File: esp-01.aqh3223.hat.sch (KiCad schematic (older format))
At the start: 17 parts, among them J1 AC Terminal, J2 GPIO/I2C, Q1 BC547, Q2 BC547, SW1 VCC_Switch, U1 ESP-01v090, U2 AMS1117-3.3, U3 AQH3223, U4 AQH3223

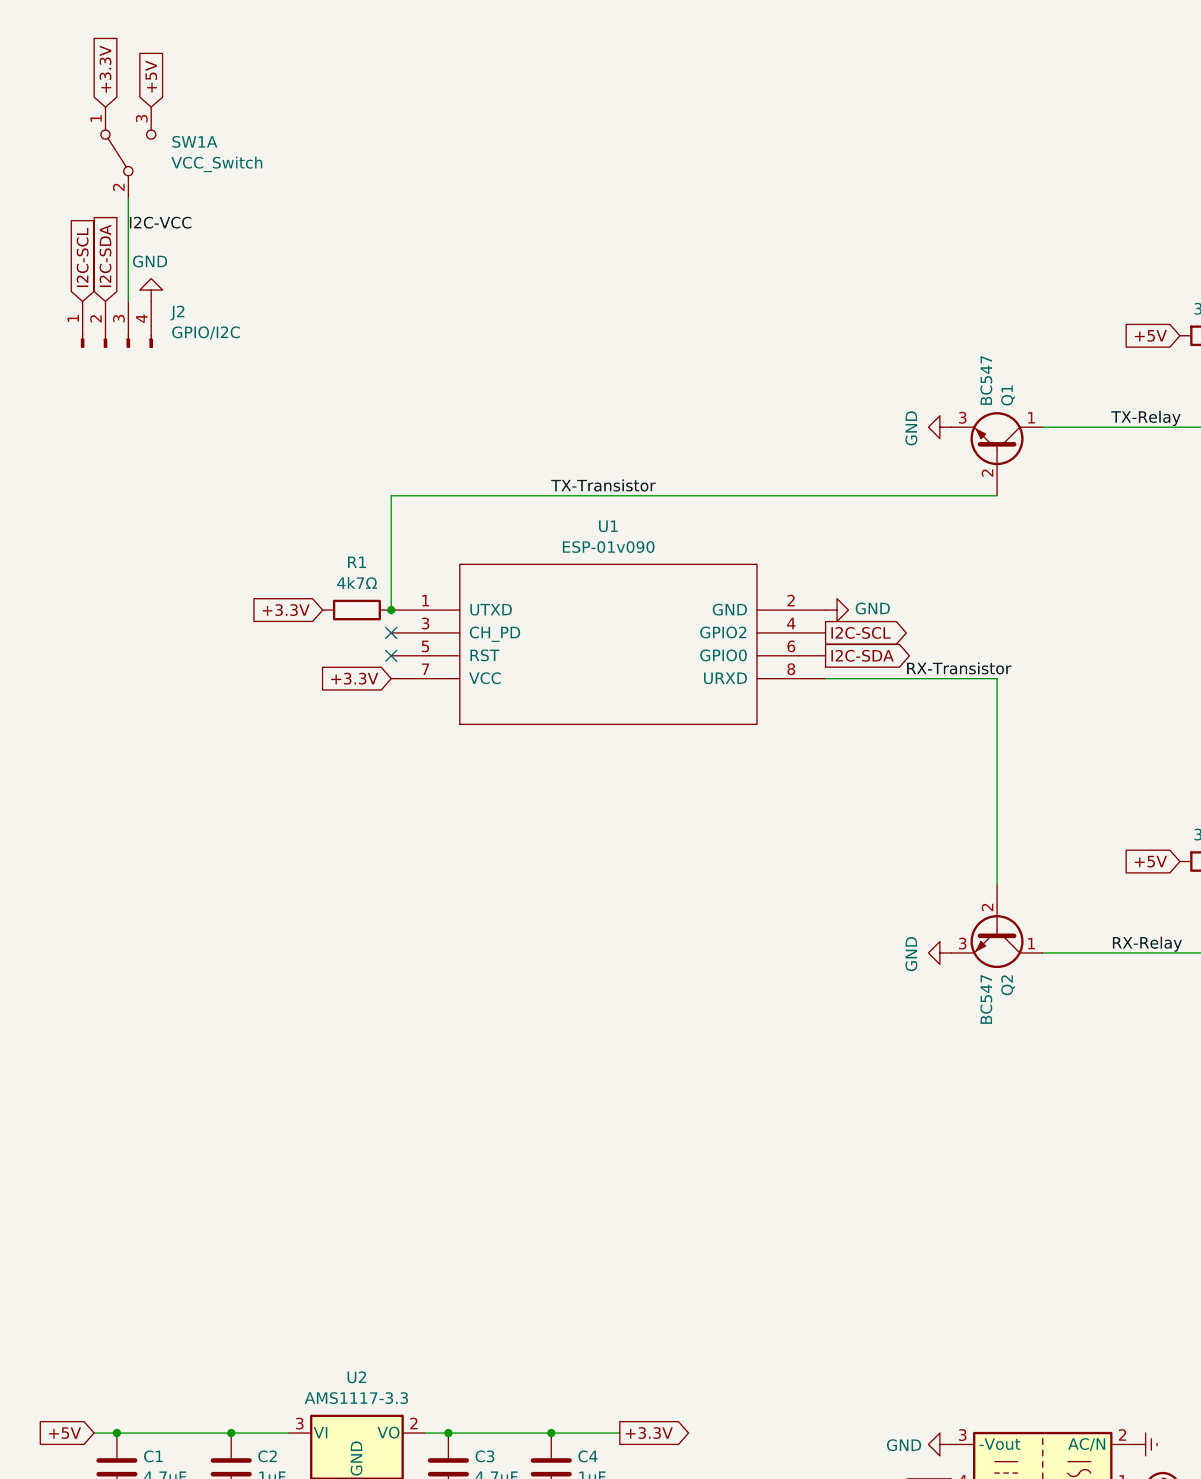
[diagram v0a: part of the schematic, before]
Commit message: fixed booting of esp-01
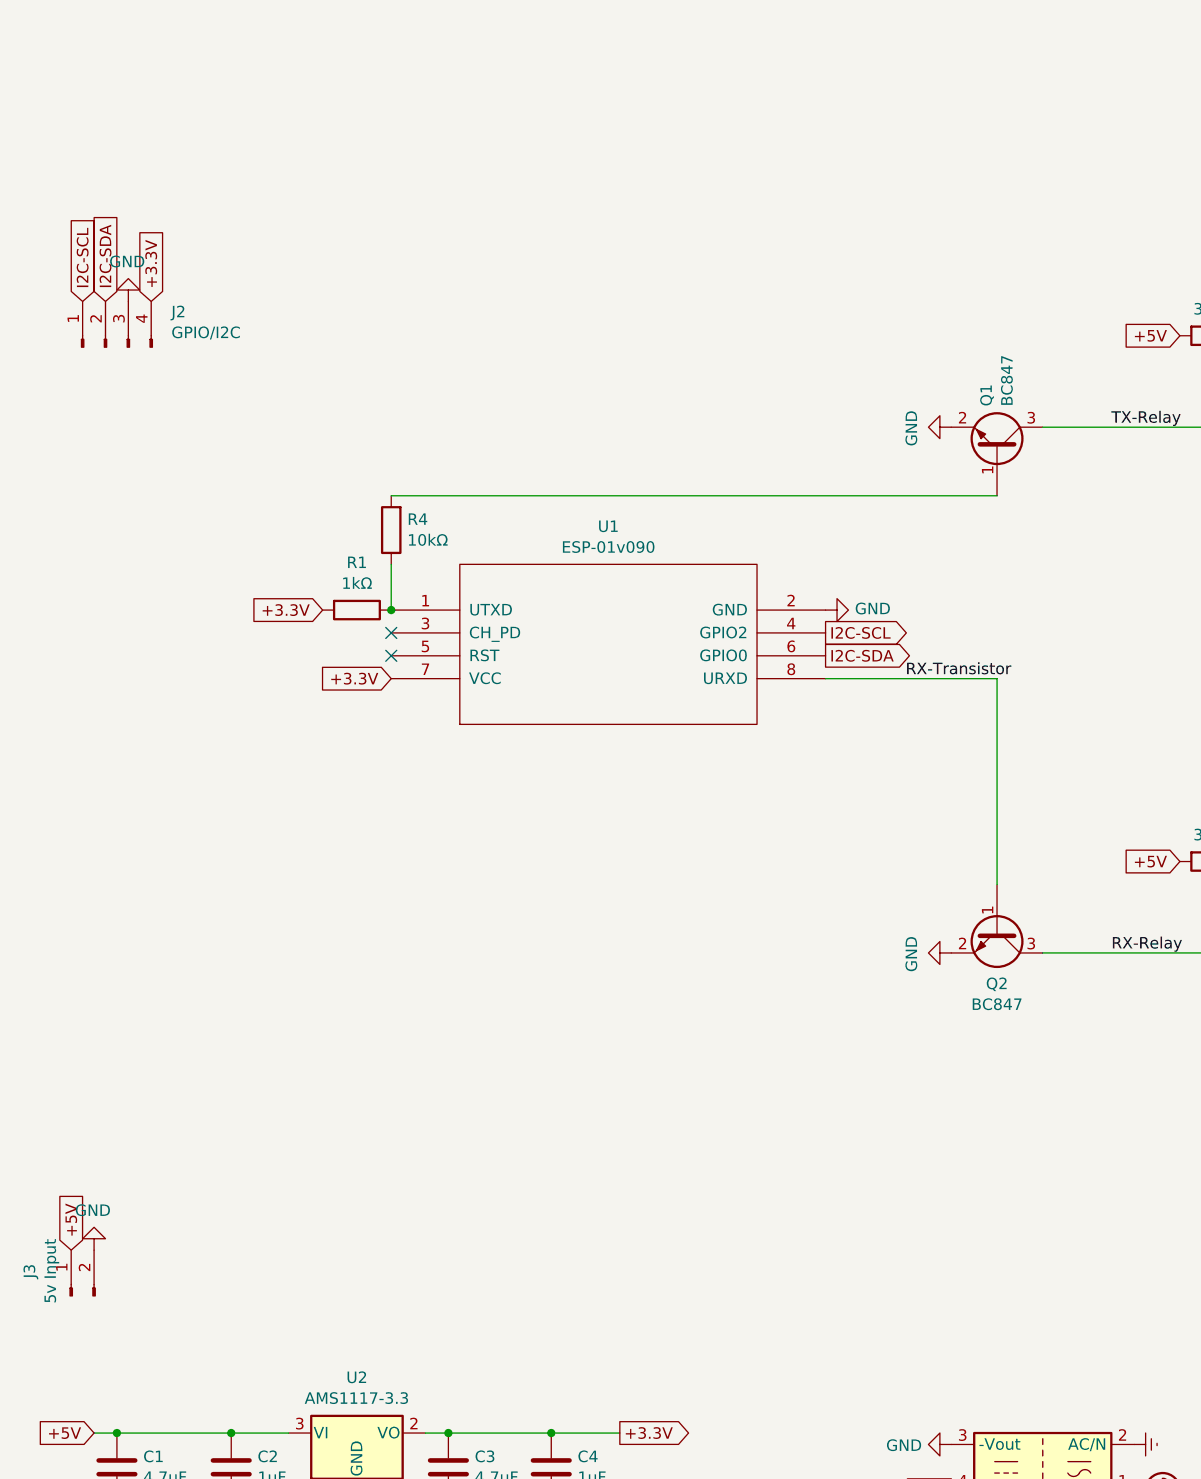
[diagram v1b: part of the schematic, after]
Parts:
- removed Q1, Q2: BC547, Package_TO_SOT_THT:TO-92_Inline, symbol Transistor_BJT:BC547
- removed SW1: VCC_Switch, Jumper:SolderJumper-3_P1.3mm_Open_Pad1.0x1.5mm, symbol Switch:SW_DPDT_x2
- added J3: 5v Input, Connector_PinSocket_2.54mm:PinSocket_1x02_P2.54mm_Vertical, symbol Connector:Conn_01x02_Male
- added Q1, Q2: BC847, Package_TO_SOT_SMD:SOT-23, symbol Transistor_BJT:BC847
- added R4: 10kΩ, Resistor_SMD:R_0805_2012Metric_Pad1.15x1.40mm_HandSolder, symbol Device:R
- J1: footprint TerminalBlock_TE-Connectivity:TerminalBlock_TE_282834-6_1x06_P2.54mm_Horizontal -> TerminalBlock:TerminalBlock_bornier-6_P5.08mm
- R1: value 4k7Ω -> 1kΩ
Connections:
- net I2C-VCC is gone; now on net GND: J2.3 (Pin_3)
- net +3.3V: now also J2.4 (Pin_4)
- net +5V: now also J3.1 (Pin_1)
- net GND: now also J3.2 (Pin_2), Q1.2 (E), Q2.2 (E); no longer J2.4 (Pin_4)
- net RX-Relay: now also Q2.3 (C)
- net RX-Transistor: now also Q2.1 (B)
- net TX-Relay: now also Q1.3 (C)
- net TX-Transistor: no longer names the net of R1.1, U1.1 (UTXD)
- net TX-Transistor: now also R4.1
- new net: Q1.1 (B), R4.2
